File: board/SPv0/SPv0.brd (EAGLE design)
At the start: 97 x 26.4 mm, 69 parts, among them IC1 S34ML0XG1, IC2 F55[0/1]X---PT48, IC3 TL084D, Q1 12MHz, T1 n3904, T2 n3904, T3 n3906, T4 n3906, T5 n3906

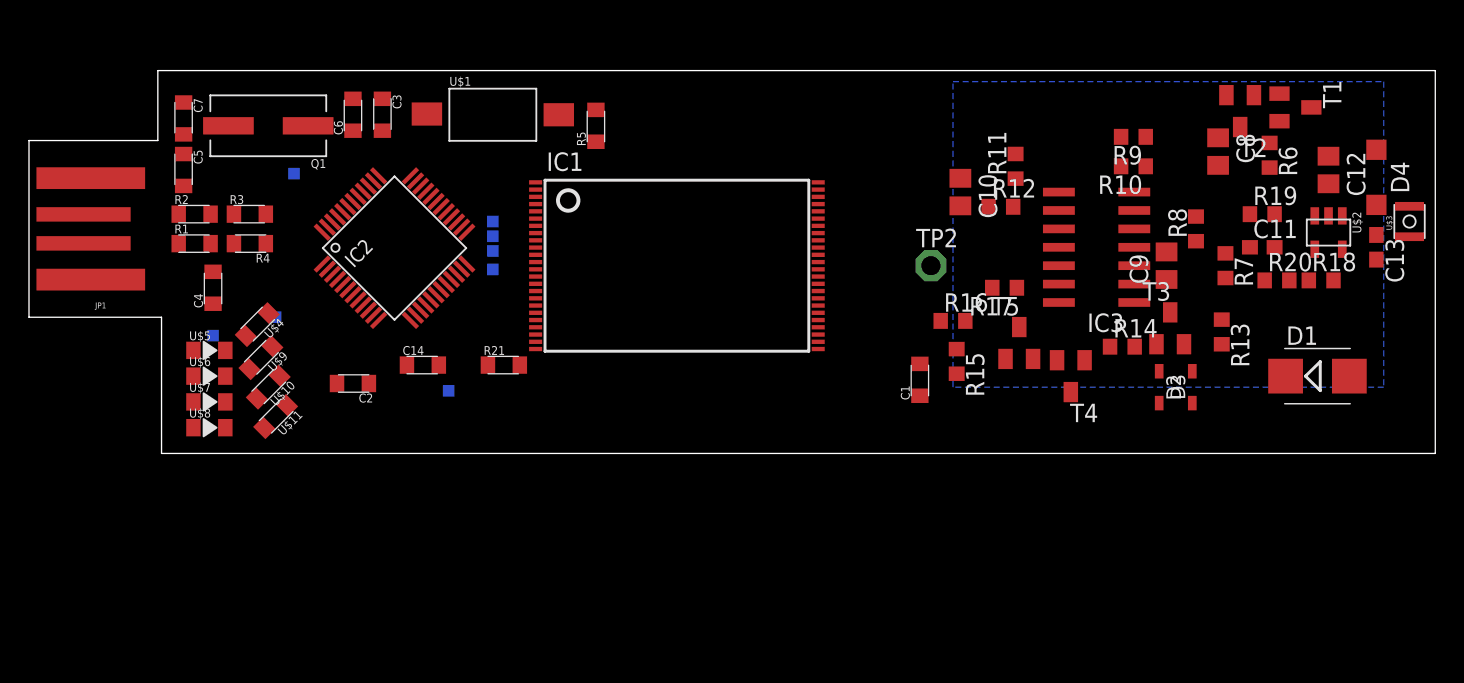
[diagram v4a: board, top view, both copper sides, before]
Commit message: added LEDs, starting layout
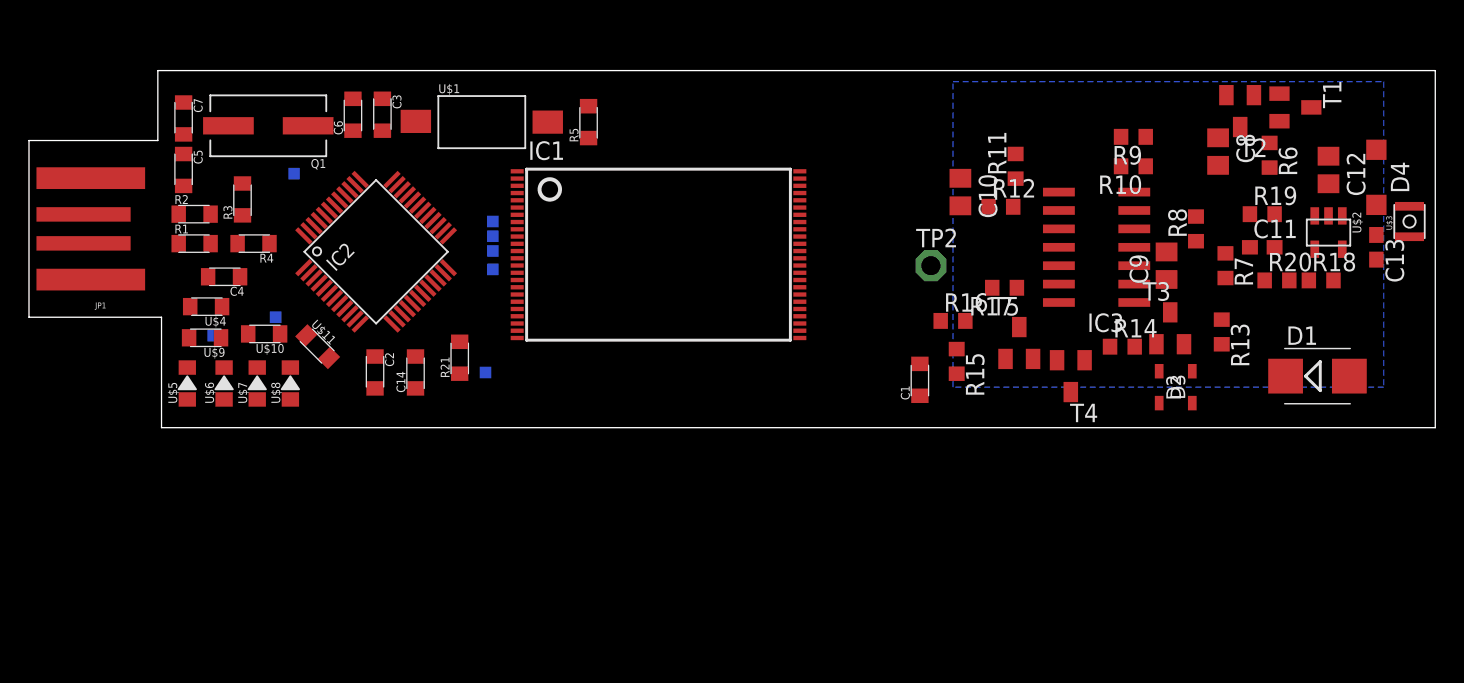
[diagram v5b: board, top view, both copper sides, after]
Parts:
- U$10, U$11, U$4, U$9: value R0805 -> 130
- moved U$8 6.37 mm to (17.5, 9.40), turned to 90 degrees
- moved U$11 5.63 mm to (19.4, 11.9), turned to 315 degrees
- moved U$9 4.09 mm to (11.6, 12.6), turned to 180 degrees
- moved U$4 3.74 mm to (11.7, 14.7), turned to 180 degrees
- moved U$10 3.68 mm to (15.7, 12.8), turned to 180 degrees
- moved U$7 3.54 mm to (15.2, 9.40), turned to 90 degrees
- moved R21 3.09 mm to (29.2, 11.2), turned to 90 degrees
- moved TP3 2.84 mm to (31.0, 10.2)
- moved U$5 2.75 mm to (10.4, 9.40), turned to 90 degrees
- moved C2 1.70 mm to (23.4, 10.2), turned to 270 degrees
- moved IC1 1.48 mm to (42.9, 18.3)
- moved IC2 1.30 mm to (23.4, 18.5)
- moved U$6 1.14 mm to (13.0, 9.40), turned to 90 degrees
- moved R3 1.14 mm to (14.2, 22.1), turned to 90 degrees
- moved C4 1.08 mm to (13.0, 16.8), turned to 180 degrees
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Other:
- board size 97 x 26.4 mm -> 97 x 24.6 mm

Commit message: added schottky diode to library fixed up led symbol swapping in sod123 diode for d1
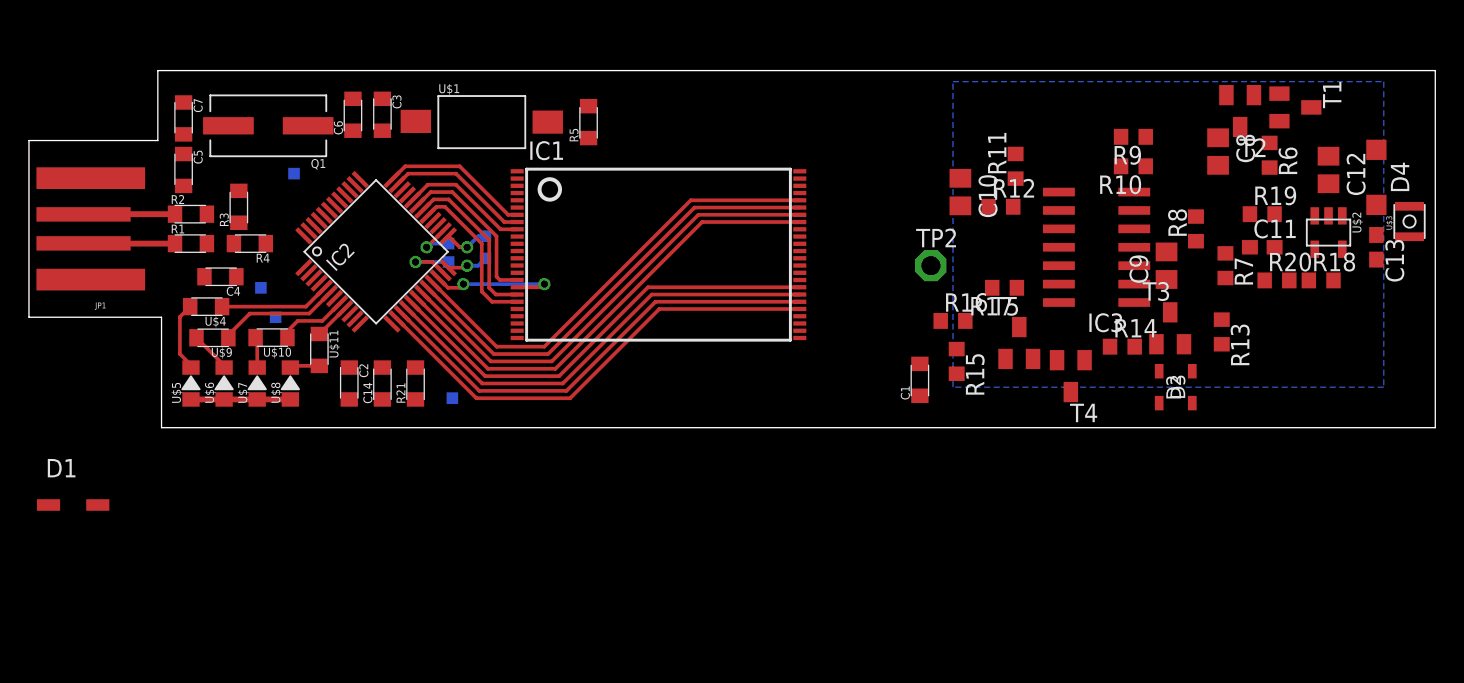
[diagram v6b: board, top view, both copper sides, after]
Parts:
- D1: device diode:SMB -> Passives:SOD123
- moved D1 86.3 mm to (2.54, 1.02)
- moved TP5 4.67 mm to (15.5, 16.0)
- moved R21 3.53 mm to (26.2, 9.40)
- moved TP6 3.41 mm to (28.4, 19.1)
- moved TP9 3.09 mm to (28.4, 17.8)
- moved TP3 2.90 mm to (28.7, 8.38)
- moved C14 2.41 mm to (23.9, 9.40)
- moved C2 1.93 mm to (21.6, 9.40)
- moved TP8 0.72 mm to (31.0, 18.0)
- moved U$10 0.57 mm to (16.2, 12.6)
- moved R3 0.57 mm to (14.0, 21.6)
- moved TP7 0.51 mm to (31.0, 19.6)
- moved U$9 0.51 mm to (12.1, 12.6)
- moved C4 0.25 mm to (12.7, 16.8)
- moved R1 0.25 mm to (10.7, 19.1)
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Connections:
- net !WE!_A: now also IC2.30; no longer IC2.31
- net !WP!_A: now also IC2.29; no longer IC2.30
- net CLE_A: now also IC2.31; no longer IC2.29
- net VBUS: now also D1.CATHODE; no longer D1.C
- net VCC: now also D1.ANODE; no longer D1.A
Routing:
- net NANDIO_A0: track 0.00 -> 32.6 mm
- net NANDIO_A4: track 0.00 -> 32.6 mm
- net NANDIO_A1: track 0.00 -> 32.2 mm
- net NANDIO_A5: track 0.00 -> 32.2 mm
- net NANDIO_A2: track 0.00 -> 31.8 mm
- net NANDIO_A6: track 0.00 -> 31.7 mm
- net NANDIO_A3: track 0.00 -> 31.3 mm
- net NANDIO_A7: track 0.00 -> 31.3 mm
- net !WE!_A: track 0.00 -> 11.5 mm
- net CLE_A: track 0.00 -> 11.4 mm
- net !WP!_A: track 0.00 -> 11.1 mm
- net R/B_A: track 0.00 -> 10.4 mm
- net !RE!_A: track 0.00 -> 9.98 mm
- net ALE_A: track 0.00 -> 9.69 mm, vias 0 -> 2
- net !CE!_A: track 0.00 -> 8.94 mm
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
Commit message: fxing up library parts added prototype for read parameter page
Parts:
- moved D1 43.3 mm to (45.0, 9.65), turned to 180 degrees
- moved C1 11.2 mm to (49.8, 10.2), turned to 270 degrees
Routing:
- net VCC: track 0.00 -> 49.1 mm, vias 0 -> 2
- net VBUS: track 0.00 -> 3.37 mm
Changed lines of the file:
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@@
 <element name="IC2" library="TI_MSP430_v16" package="PT48" value="F55[0/1]X---PT48" x="23.442396875" y="18.48565625" rot="R45"/>
 <element name="JP1" library="SparkFun-Connectors" package="USB-A-PCB" value="USBPCB" x="3.556" y="20.066" rot="R180"/>
-<element name="C1" library="Passives" package="R0805" value="4.7uF" x="60.96" y="9.652" rot="R90"/>
+<element name="C1" library="Passives" package="R0805" value="4.7uF" x="49.784" y="10.16" rot="R270"/>
 <element name="C2" library="Passives" package="R0805" value="220nF" x="21.59" y="9.398" rot="R270"/>
 <element name="C3" library="Passives" package="R0805" value="220nF" x="23.876" y="27.94" rot="R270"/>
@@
 <element name="U$10" library="Passives" package="R0805" value="130" x="16.225184375" y="12.563971875" rot="R180"/>
 <element name="U$11" library="Passives" package="R0805" value="130" x="19.527178125" y="11.714815625" rot="R270"/>
-<element name="D1" library="Passives" package="SOD123" value="" x="2.54" y="1.016"/>
+<element name="D1" library="Passives" package="SOD123" value="" x="44.958" y="9.652" rot="R180"/>
 </elements>
 <signals>
@@
 <wire x1="64.096" y1="13.716" x2="70.552" y2="16.256" width="0" layer="19" extent="1-1"/>
 <wire x1="63.5" y1="11.772" x2="64.096" y2="13.716" width="0" layer="19" extent="1-1"/>
-<wire x1="60.96" y1="8.552" x2="63.5" y2="11.772" width="0" layer="19" extent="1-1"/>
-<wire x1="52.676" y1="12.538" x2="60.96" y2="8.552" width="0" layer="19" extent="1-1"/>
+<wire x1="49.784" y1="11.26" x2="63.5" y2="11.772" width="0" layer="19" extent="1-1"/>
+<wire x1="52.676" y1="12.538" x2="49.784" y2="11.26" width="0" layer="19" extent="1-1"/>
 <wire x1="27.720390625" y1="20.288778125" x2="33.176" y2="18.038" width="0" layer="19" extent="1-1"/>
 <wire x1="22.34638125" y1="23.47075625" x2="27.720390625" y2="20.288778125" width="0" layer="19" extent="1-1"/>
@@
 <wire x1="13.8" y1="16.764" x2="13.97" y2="22.69" width="0" layer="19" extent="1-1"/>
 <wire x1="15.494" y1="16.002" x2="13.8" y2="16.764" width="0" layer="19" extent="1-16"/>
-<wire x1="3.756" y1="23.566" x2="10.16" y2="25.23" width="0" layer="19" extent="1-1"/>
-<wire x1="21.639271875" y1="14.207659375" x2="19.87150625" y2="20.995884375" width="0" layer="19" extent="1-1"/>
+<wire x1="21.639271875" y1="14.207659375" x2="15.494" y2="16.002" width="0" layer="19" extent="1-16"/>
 <wire x1="22.34638125" y1="13.500553125" x2="21.639271875" y2="14.207659375" width="0" layer="19" extent="1-1"/>
 <wire x1="21.59" y1="10.498" x2="22.34638125" y2="13.500553125" width="0" layer="19" extent="1-1"/>
 <wire x1="23.876" y1="8.298" x2="21.59" y2="10.498" width="0" layer="19" extent="1-1"/>
+<wire x1="3.756" y1="23.566" x2="10.16" y2="25.23" width="0" layer="19" extent="1-1"/>
 </signal>
 <signal name="+3V3_A">
@@
 <contactref element="U$6" pad="ANODE"/>
 <contactref element="U$7" pad="ANODE"/>
+<wire x1="10.668" y1="8.298" x2="12.954" y2="8.298" width="0.4064" layer="1"/>
+<wire x1="12.954" y1="8.298" x2="15.24" y2="8.298" width="0.4064" layer="1"/>
+<wire x1="15.24" y1="8.298" x2="17.526" y2="8.298" width="0.4064" layer="1"/>
 <wire x1="33.176" y1="18.538" x2="38.1" y2="26.332" width="0" layer="19" extent="1-1"/>
 <wire x1="27.3668375" y1="20.64233125" x2="33.176" y2="18.538" width="0" layer="19" extent="1-1"/>
@@
 <wire x1="26.162" y1="8.298" x2="21.59" y2="8.298" width="0" layer="19" extent="1-1"/>
 <wire x1="28.702" y1="8.382" x2="26.162" y2="8.298" width="0" layer="19" extent="1-16"/>
-<wire x1="10.668" y1="8.298" x2="12.954" y2="8.298" width="0.4064" layer="1"/>
-<wire x1="12.954" y1="8.298" x2="15.24" y2="8.298" width="0.4064" layer="1"/>
-<wire x1="15.24" y1="8.298" x2="17.526" y2="8.298" width="0.4064" layer="1"/>
 </signal>
 <signal name="VBUS">
@@
 <contactref element="C1" pad="P$1"/>
 <contactref element="D1" pad="CATHODE"/>
-<wire x1="20.932165625" y1="22.05654375" x2="60.96" y2="10.752" width="0" layer="19" extent="1-1"/>
-<wire x1="0.84" y1="1.016" x2="20.932165625" y2="22.05654375" width="0" layer="19" extent="1-1"/>
+<wire x1="46.658" y1="9.652" x2="47.25" y2="9.06" width="0.6096" layer="1"/>
+<wire x1="47.25" y1="9.06" x2="49.784" y2="9.06" width="0.6096" layer="1"/>
+<wire x1="20.932165625" y1="22.05654375" x2="46.658" y2="9.652" width="0" layer="19" extent="1-1"/>
 </signal>
 <signal name="+1V8_A">
@@
 <contactref element="TP4" pad="TP"/>
 <contactref element="R21" pad="P$1"/>
-<wire x1="16.51" y1="13.97" x2="26.162" y2="10.498" width="0" layer="19" extent="1-16"/>
-<wire x1="18.45729375" y1="19.58166875" x2="16.51" y2="13.97" width="0" layer="19" extent="1-16"/>
+<wire x1="16.51" y1="13.97" x2="18.45729375" y2="19.58166875" width="0" layer="19" extent="1-16"/>
+<wire x1="26.162" y1="10.498" x2="16.51" y2="13.97" width="0" layer="19" extent="1-16"/>
 </signal>
 <signal name="TST_A">
@@
 <wire x1="92.456" y1="17.946" x2="94.742" y2="19.524" width="0" layer="19" extent="1-1"/>
 <wire x1="90.104" y1="18.662" x2="92.456" y2="17.946" width="0" layer="19" extent="1-1"/>
-<wire x1="3.756" y1="16.566" x2="90.104" y2="18.662" width="0" layer="19" extent="1-1"/>
-<wire x1="4.24" y1="1.016" x2="3.756" y2="16.566" width="0" layer="19" extent="1-1"/>
+<wire x1="43.258" y1="9.652" x2="90.104" y2="18.662" width="0" layer="19" extent="1-1"/>
+<wire x1="3.756" y1="16.566" x2="3.954" y2="16.764" width="0.6096" layer="1"/>
+<wire x1="3.954" y1="16.764" x2="9.906" y2="16.764" width="0.6096" layer="1"/>
+<via x="9.906" y="16.764" extent="1-16" drill="0.5"/>
+<wire x1="9.906" y1="16.764" x2="10.668" y2="16.002" width="0.6096" layer="16"/>
+<wire x1="10.668" y1="16.002" x2="10.668" y2="8.382" width="0.6096" layer="16"/>
+<wire x1="10.668" y1="8.382" x2="10.922" y2="8.128" width="0.6096" layer="16"/>
+<wire x1="10.922" y1="8.128" x2="43.18" y2="8.128" width="0.6096" layer="16"/>
+<via x="43.18" y="8.128" extent="1-16" drill="0.5"/>
+<wire x1="43.18" y1="8.128" x2="43.18" y2="8.89" width="0.6096" layer="1"/>
+<wire x1="43.18" y1="8.89" x2="43.258" y2="8.968" width="0.6096" layer="1"/>
+<wire x1="43.258" y1="8.968" x2="43.258" y2="9.652" width="0.6096" layer="1"/>
 </signal>
 <signal name="N$5">
@@
 <contactref element="C14" pad="P$1"/>
 <contactref element="IC2" pad="13"/>
-<wire x1="24.538409375" y1="13.500553125" x2="23.876" y2="10.498" width="0" layer="19" extent="1-1"/>
+<wire x1="23.876" y1="10.498" x2="24.538409375" y2="13.500553125" width="0" layer="19" extent="1-1"/>
 </signal>
 <signal name="N$22">

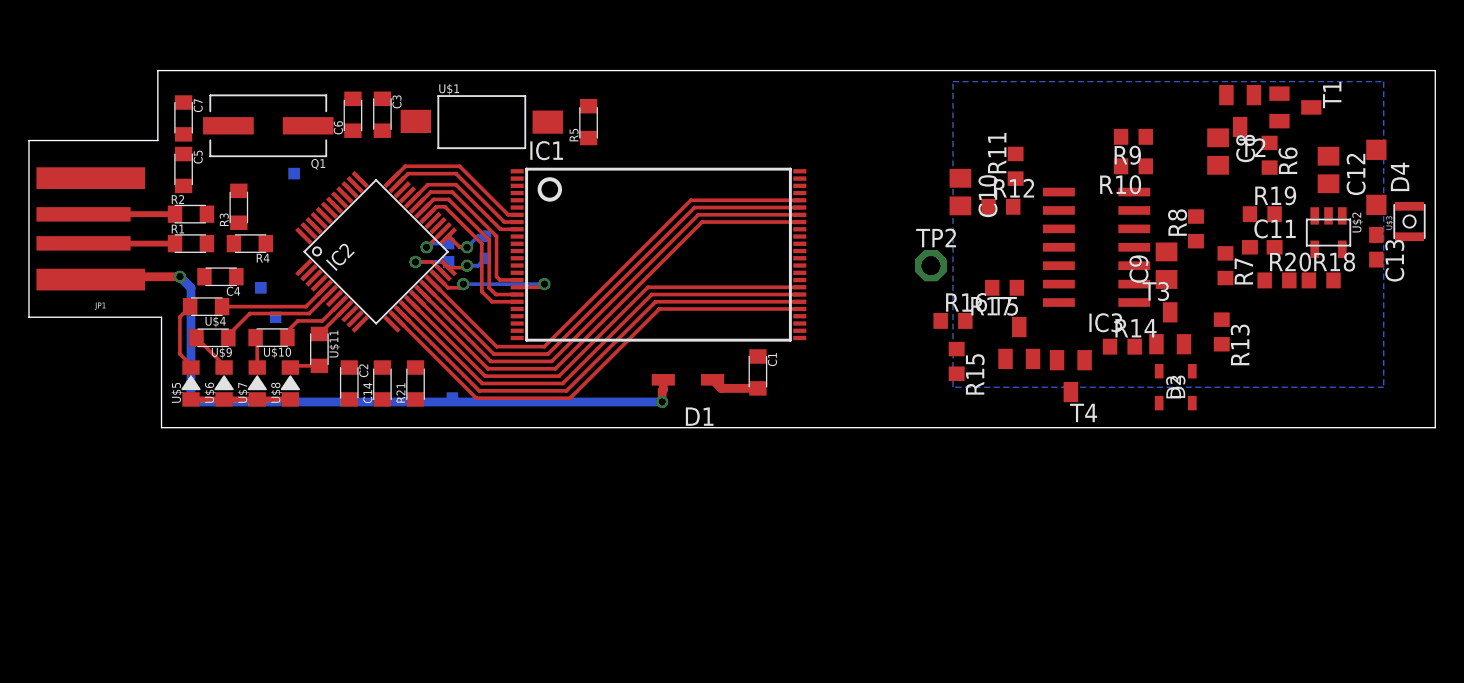
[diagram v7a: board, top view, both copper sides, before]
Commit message: 1/2 board w/ new rng done. needs test points, confirm switch
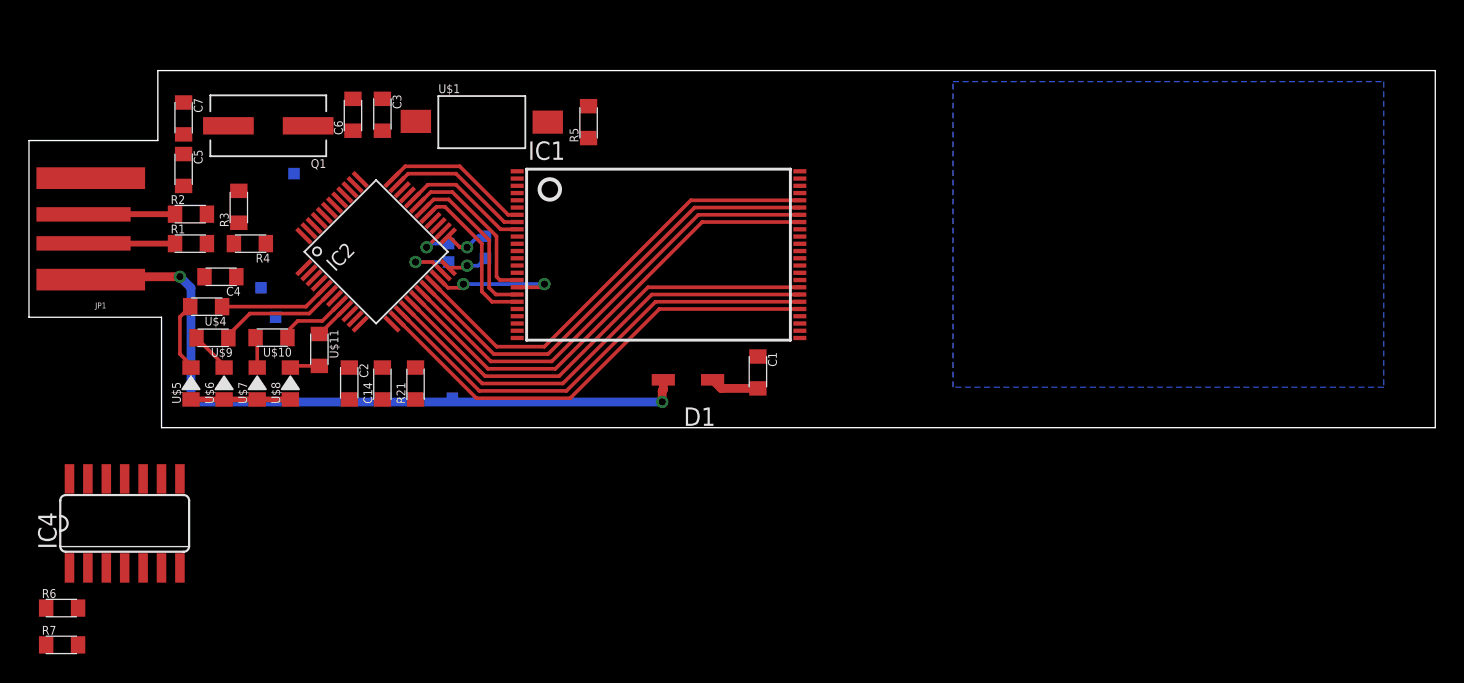
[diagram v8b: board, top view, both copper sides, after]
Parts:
- removed C10: 4.7u, rcl:C0805
- removed C11: 120pF, rcl:C0603
- removed C12: 4.7uF, rcl:C0805
- removed C13: 2.2uF, rcl:C0603
- removed C8, C9: 0.47u, rcl:C0805
- removed D2, D3: 1n4148, zetex:SOD323
- removed D4: (no value), diode:SOD123
- removed IC3: TL084D, linear:SO14
- removed R10: 1M, rcl:R0603
- removed R11, R12: 100K, rcl:R0603
- removed R13: 1.2K, rcl:R0603
- removed R14, R15: 10K, rcl:R0603
- removed R16, R17: 5K, rcl:R0603
- removed R18: 51K, rcl:R0603
- removed R19: 205K, rcl:R0603
- removed R20: 13.3K, rcl:R0603
- removed R8: 12K, rcl:R0603
- removed R9: 47K, rcl:R0603
- removed T1, T2: n3904, transistor:SOT23-BEC
- removed T3, T4, T5: n3906, transistor:SOT23-BEC
- removed TP2: PTR1PAD1-13, testpad:P1-13
- removed U$2: LM27313, rng:SOT-23-5
- removed U$3: 10uH, rng:L1007
- added IC4: 74LS14D, 74xx-us:SO14
- R6: value 150K -> 1.4k; device rcl:R0603 -> Passives:R0805
- R7: value 1M -> 1.4k; device rcl:R0603 -> Passives:R0805
- moved R6 89.0 mm to (1.78, -6.10), turned to 0 degrees
- moved R7 84.4 mm to (1.78, -8.64), turned to 0 degrees
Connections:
- removed net AOUT: IC3.7, R9.2, T5.B
- removed net N$11: IC3.5, R10.1
- removed net N$12: C10.1, IC3.10, R11.1, R12.2
- removed net N$13: D3.1, R14.2, T3.B
- removed net N$14: D2.1, D3.2
- removed net N$15: R13.1, T3.E
- removed net N$16: T3.C, T4.E, T5.E
- removed net N$17: R15.2, T4.C
- removed net N$18: R17.1, T5.C
- removed net N$20: D4.A, U$2.P$1, U$3.P$2
- removed net N$21: C11.2, R19.2, R20.1, U$2.P$3
- removed net VDD: C11.1, C12.1, D2.2, D4.C, IC3.4, R11.2, R13.2, R19.1, R6.2
- removed net VREF: IC3.8, IC3.9, R10.2, R7.2, T4.B
- net !VDD_SHDN!: no longer R18.2, U$2.P$4
- net DOUT: now also R6.P$1, R7.P$2; no longer R16.1, R17.2, TP2.TP
- net GND: now also IC4.7, R7.P$1; no longer C10.2, C12.2, C13.1, IC3.11, IC3.12, IC3.13, R12.1, R14.1, R15.1, R16.2, R18.1, R20.2, T2.E, U$2.P$2
- net N$10: now also IC4.6, R6.P$2; no longer IC3.6, R8.2, R9.1
- net N$5: now also IC4.11, IC4.12; no longer C8.1, R6.1, T1.E, T2.C
- net N$6: now also IC4.10, IC4.9; no longer T1.B, T2.B
- net N$7: now also IC4.1, IC4.8; no longer C8.2, IC3.3, R7.1
- net N$8: now also IC4.2, IC4.3; no longer C9.1, IC3.1, IC3.2
- net N$9: now also IC4.13, IC4.4, IC4.5; no longer C9.2, R8.1
- net VCC: now also IC4.14; no longer C13.2, U$2.P$5, U$3.P$1
